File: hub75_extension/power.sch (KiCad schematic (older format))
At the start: 13 parts, among them J1 Screw_Terminal_01x02, J2 Screw_Terminal_01x02, J3 Barrel_Jack_Switch, J4 Screw_Terminal_01x02, J5 Screw_Terminal_01x02, J6 Barrel_Jack_Switch, J7 Screw_Terminal_01x02, J8 Screw_Terminal_01x02, J9 USB_B_Micro, U2 EBay special DCDC

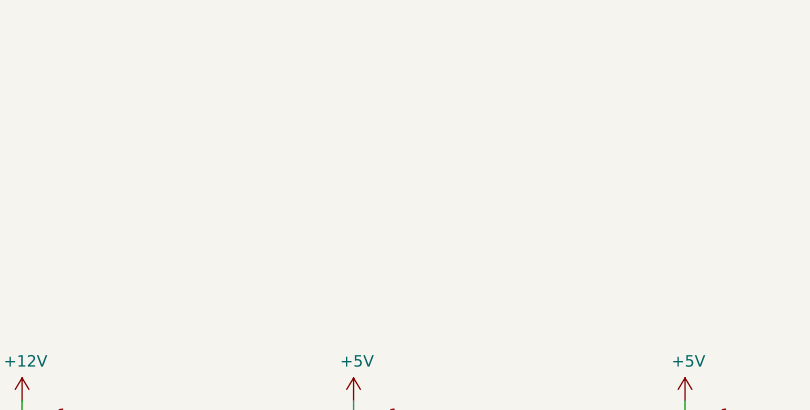
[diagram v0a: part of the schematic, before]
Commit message: Add some spare footprints, just in case
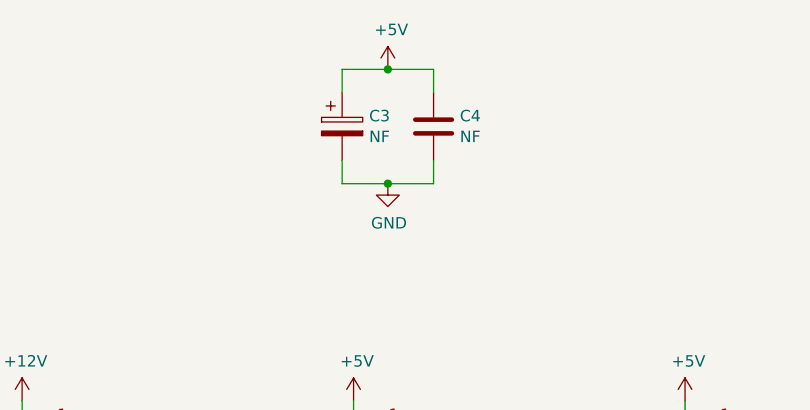
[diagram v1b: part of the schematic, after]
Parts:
- added C3: NF, symbol Device:CP
- added C4: NF, symbol Device:C
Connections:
- net +5V: now also C3.1, C4.1
- net GND: now also C3.2, C4.2
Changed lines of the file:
@@
 	1    0    0    -1
 $EndComp
+$Comp
+L Device:CP C3
+U 1 1 60832C4F
+P 8200 2750
+F 0 "C3" H 8318 2796 50  0000 L CNN
+F 1 "NF" H 8318 2705 50  0000 L CNN
+F 2 "" H 8238 2600 50  0001 C CNN
+F 3 "~" H 8200 2750 50  0001 C CNN
+	1    8200 2750
+	1    0    0    -1
+$EndComp
+$Comp
+L Device:C C4
+U 1 1 60837FCC
+P 8600 2750
+F 0 "C4" H 8715 2796 50  0000 L CNN
+F 1 "NF" H 8715 2705 50  0000 L CNN
+F 2 "" H 8638 2600 50  0001 C CNN
+F 3 "~" H 8600 2750 50  0001 C CNN
+	1    8600 2750
+	1    0    0    -1
+$EndComp
+$Comp
+L power:+5V #PWR050
+U 1 1 60838C23
+P 8400 2500
+F 0 "#PWR050" H 8400 2350 50  0001 C CNN
+F 1 "+5V" H 8415 2673 50  0000 C CNN
+F 2 "" H 8400 2500 50  0001 C CNN
+F 3 "" H 8400 2500 50  0001 C CNN
+	1    8400 2500
+	1    0    0    -1
+$EndComp
+Wire Wire Line
+	8200 2600 8200 2500
+Wire Wire Line
+	8200 2500 8400 2500
+Wire Wire Line
+	8600 2500 8600 2600
+Connection ~ 8400 2500
+Wire Wire Line
+	8400 2500 8600 2500
+Wire Wire Line
+	8200 2900 8200 3000
+Wire Wire Line
+	8200 3000 8400 3000
+Wire Wire Line
+	8600 3000 8600 2900
+$Comp
+L power:GND #PWR051
+U 1 1 6083BB07
+P 8400 3000
+F 0 "#PWR051" H 8400 2750 50  0001 C CNN
+F 1 "GND" H 8405 2827 50  0000 C CNN
+F 2 "" H 8400 3000 50  0001 C CNN
+F 3 "" H 8400 3000 50  0001 C CNN
+	1    8400 3000
+	1    0    0    -1
+$EndComp
+Connection ~ 8400 3000
+Wire Wire Line
+	8400 3000 8600 3000
 $EndSCHEMATC

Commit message: Yeah, just renumber the entire thing...
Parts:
- renumbered C3 to C201, C4 to C202, H1 to H201, H2 to H202, H3 to H203, J1 to J201, J2 to J202, J3 to J203, J4 to J204, J5 to J205, J6 to J206, J7 to J207, J8 to J208, J9 to J209, U2 to U201
